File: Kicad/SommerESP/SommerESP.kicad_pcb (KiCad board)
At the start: 2 copper layers, 76.8 x 23.5 mm, 31 parts, among them J1 Serial programmer, J3 SOMMER CONEX BOARD, J4 SOMMER CONEX KEYPAD, J6 SOMMER OUTPUT OC, Q1 STN3NF06, Q2 2N7002DW, U4 LM2596SX-3.3/NOPB, U5 ESP32-C3-WROOM-02

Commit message: Fixed wrong LCSC number on the BOM
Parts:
- D1: value LED Green -> LED
- D2: value LED Blue -> LED
- turned C3 to 180 degrees

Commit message: Added 7.5mm position for J7 for more compatibility and updated the readme
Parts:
- added J7: SOMMER OUTPUT OC 7.5mm, Connector_PinSocket_2.54mm:PinSocket_1x04_P2.54mm_Vertical, B.Cu at (65.7, 36.7)
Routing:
- net GND: track 30.4 -> 32.4 mm
- net SommerSIG: track 7.28 -> 8.53 mm
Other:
- board text added: "7.5"
- board text added: "9.5"
- board text added: "SommerESP V3.1"
- board text added: "SommerESP v3.1"
- board text added: "X"
- board text removed: "SommerESP V3"
- board text removed: "SommerESP v3.0"

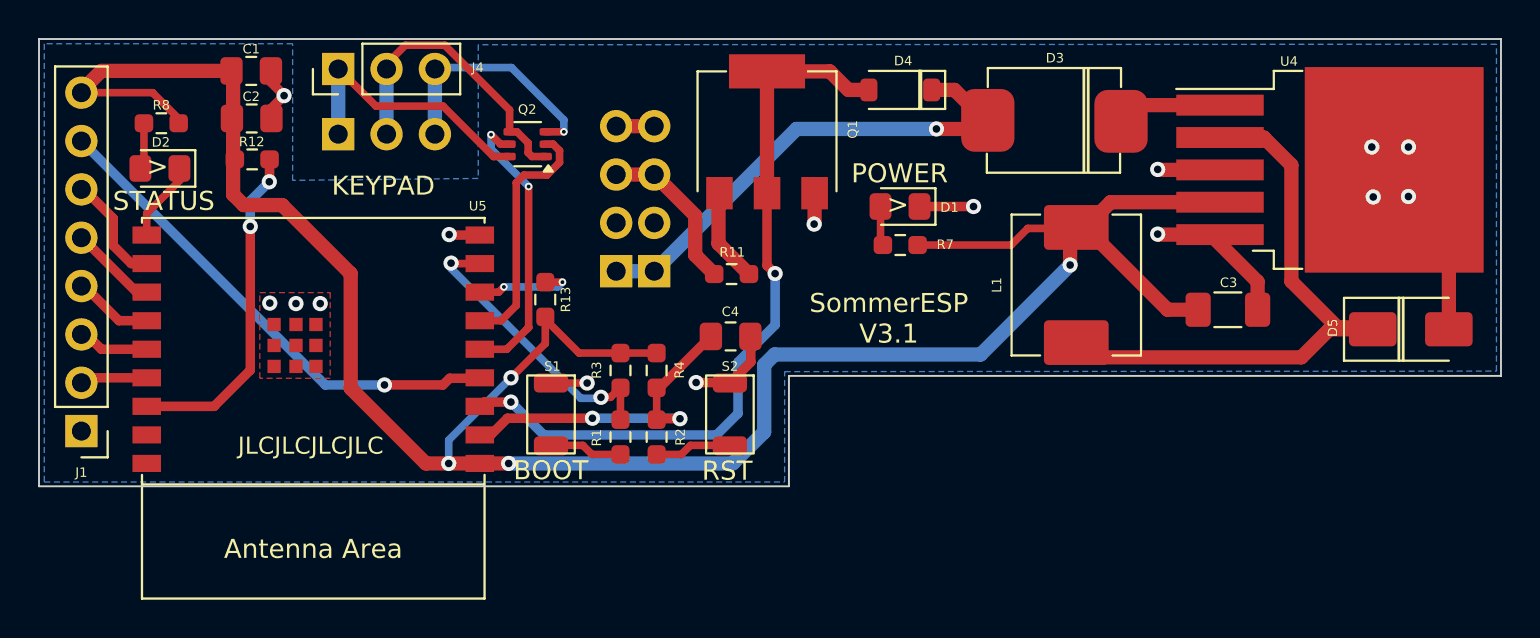
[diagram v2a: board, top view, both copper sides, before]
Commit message: Added fabrication holes on the PCB and setup up for production.
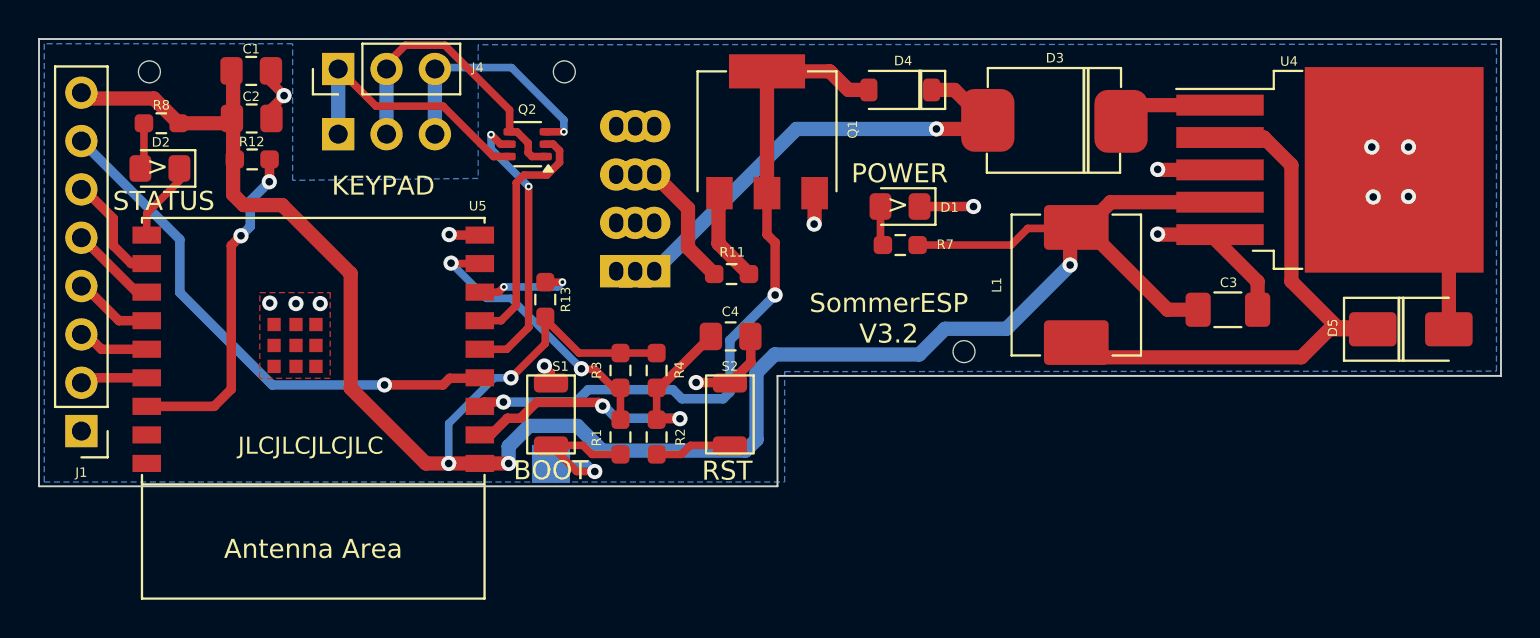
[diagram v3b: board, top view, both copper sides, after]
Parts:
- added H1: MountingHole, MountingHole:ToolingHole_1.152mm, F.Cu at (82.0, 40.9)
- added H2: MountingHole, MountingHole:ToolingHole_1.152mm, F.Cu at (39.2, 26.2)
- added H3: MountingHole, MountingHole:ToolingHole_1.152mm, F.Cu at (61.0, 26.2)
- added J8: SOMMER OUTPUT OC 8.5mm, SommerCustom:PinSocket_1x04_P2.54mm_Vertical_SLIT, B.Cu at (64.7, 36.7)
- added TP1: TestPoint, TestPoint:TestPoint_Pad_2.0x2.0mm, B.Cu at (60.3, 46.8)
- J6: value SOMMER OUTPUT OC -> SOMMER OUTPUT OC 9.5; footprint Connector_PinSocket_2.54mm:PinSocket_1x04_P2.54mm_Vertical -> SommerCustom:PinSocket_1x04_P2.54mm_Vertical_SLIT
- J7: footprint Connector_PinSocket_2.54mm:PinSocket_1x04_P2.54mm_Vertical -> SommerCustom:PinSocket_1x04_P2.54mm_Vertical_SLIT
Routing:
- net Net-(R1-Pad1): track 3.67 -> 9.00 mm, vias 0 -> 1
- net +3.3V: track 120.3 -> 117.2 mm
- net GND: track 32.4 -> 29.8 mm
- net AnalogSIG: track 37.6 -> 35.6 mm
- net IO5: track 26.1 -> 27.7 mm
- net EN: track 17.5 -> 18.2 mm
- net IO9: track 15.1 -> 14.6 mm
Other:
- outline, holes or cut-outs redrawn
- board text added: "8.5"
- board text added: "SommerESP V3.2"
- board text added: "SommerESP v3.2"
- board text removed: "SommerESP V3.1"
- board text removed: "SommerESP v3.1"

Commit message: Added RST pad
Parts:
- added TP2: RST, TestPoint:TestPoint_Pad_2.0x2.0mm, B.Cu at (69.7, 46.8)
- TP1: value TestPoint -> BOOT
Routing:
- net Net-(R2-Pad1): track 4.00 -> 8.45 mm, vias 0 -> 1
- net +3.3V: track 117.2 -> 115.4 mm
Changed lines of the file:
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@@
 		(embedded_fonts no)
 	)
+	(footprint "TestPoint:TestPoint_Pad_2.0x2.0mm"
+		(layer "B.Cu")
+		(at 69.725 46.825 180)
+		(descr "SMD rectangular pad as test Point, square 2.0mm side length")
+		(tags "test point SMD pad rectangle square")
+		(property "Reference" "TP2"
+			(at 0 1.998 0)
+			(layer "B.SilkS")
+			(hide yes)
+			(effects
+				(font
+					(size 1 1)
+					(thickness 0.15)
+				)
+				(justify mirror)
+			)
+		)
+		(property "Value" "RST"
+			(at 0 -2.05 0)
+			(layer "B.Fab")
+			(effects
+				(font
+					(size 1 1)
+					(thickness 0.15)
+				)
+				(justify mirror)
+			)
+		)
+		(property "Datasheet" ""
+			(at 0 0 0)
+			(unlocked yes)
+			(layer "B.Fab")
+			(hide yes)
+			(effects
+				(font
+					(size 1.27 1.27)
+					(thickness 0.15)
+				)
+				(justify mirror)
+			)
+		)
+		(property "Description" "test point"
+			(at 0 0 0)
+			(unlocked yes)
+			(layer "B.Fab")
+			(hide yes)
+			(effects
+				(font
+					(size 1.27 1.27)
+					(thickness 0.15)
+				)
+				(justify mirror)
+			)
+		)
+		(property ki_fp_filters "Pin* Test*")
+		(sheetname "/")
+		(sheetfile "SommerESP.kicad_sch")
+		(units
+			(unit
+				(name "A")
+				(pins "1")
+			)
+		)
+		(duplicate_pad_numbers_are_jumpers no)
+		(fp_line
+			(start 1.2 1.2)
+			(end 1.2 -1.2)
+			(stroke
+				(width 0.12)
+				(type solid)
+			)
+			(layer "B.SilkS")
+		)
+		(fp_line
+			(start 1.2 -1.2)
+			(end -1.2 -1.2)
+			(stroke
+				(width 0.12)
+				(type solid)
+			)
+			(layer "B.SilkS")
+		)
+		(fp_line
+			(start -1.2 1.2)
+			(end 1.2 1.2)
+			(stroke
+				(width 0.12)
+				(type solid)
+			)
+			(layer "B.SilkS")
+		)
+		(fp_line
+			(start -1.2 -1.2)
+			(end -1.2 1.2)
+			(stroke
+				(width 0.12)
+				(type solid)
+			)
+			(layer "B.SilkS")
+		)
+		(fp_line
+			(start 1.5 -1.5)
+			(end 1.5 1.5)
+			(stroke
+				(width 0.05)
+				(type solid)
+			)
+			(layer "B.CrtYd")
+		)
+		(fp_line
+			(start 1.5 -1.5)
+			(end -1.5 -1.5)
+			(stroke
+				(width 0.05)
+				(type solid)
+			)
+			(layer "B.CrtYd")
+		)
+		(fp_line
+			(start -1.5 1.5)
+			(end 1.5 1.5)
+			(stroke
+				(width 0.05)
+				(type solid)
+			)
+			(layer "B.CrtYd")
+		)
+		(fp_line
+			(start -1.5 1.5)
+			(end -1.5 -1.5)
+			(stroke
+				(width 0.05)
+				(type solid)
+			)
+			(layer "B.CrtYd")
+		)
+		(fp_text user "${REFERENCE}"
+			(at 0 2 0)
+			(layer "B.Fab")
+			(effects
+				(font
+					(size 1 1)
+					(thickness 0.15)
+				)
+				(justify mirror)
+			)
+		)
+		(pad "1" smd rect
+			(at 0 0 180)
+			(size 2 2)
+			(layers "B.Cu" "B.Mask")
+			(net "Net-(R2-Pad1)")
+			(pinfunction "1_1")
+			(pintype "passive")
+		)
+		(embedded_fonts no)
+	)
 	(footprint "LOGO"
 		(layer "B.Cu")
@@
 			)
 		)
-		(property "Value" "TestPoint"
+		(property "Value" "BOOT"
 			(at 0 -2.05 0)
 			(layer "B.Fab")
@@
 		)
 	)
-	(gr_text "BOOT\n"
-		(at 62.2 45.5 0)
-		(layer "B.SilkS")
-		(effects
-			(font
-				(size 1 1)
-				(thickness 0.15)
-			)
-			(justify left bottom mirror)
-		)
-	)
 	(gr_text "SommerESP v3.2\n"
-		(at 51.6 37.6 0)
+		(at 51.8 35.1 0)
 		(layer "B.SilkS")
 		(effects
@@
 	)
 	(segment
-		(start 71.1 42)
-		(end 72.05 41.05)
+		(start 68.45 44.8)
+		(end 69.5 44.8)
 		(width 0.75)
 		(layer "B.Cu")
@@
 	)
 	(segment
-		(start 62.986626 46.101)
-		(end 70.524 46.101)
+		(start 84.525 39.4)
+		(end 87.575 36.35)
 		(width 0.75)
 		(layer "B.Cu")
@@
 	)
 	(segment
-		(start 71.1 45.525)
-		(end 71.1 42)
+		(start 59.15 44.8)
+		(end 61.685626 44.8)
 		(width 0.75)
 		(layer "B.Cu")
@@
 	)
 	(segment
-		(start 61.685626 44.8)
-		(end 62.986626 46.101)
+		(start 69.5 44.8)
+		(end 71.1 43.2)
 		(width 0.75)
 		(layer "B.Cu")
@@
 	)
 	(segment
-		(start 58.075 45.875)
-		(end 59.15 44.8)
+		(start 61.685626 44.8)
+		(end 62.385626 45.5)
 		(width 0.75)
 		(layer "B.Cu")
@@
 	)
 	(segment
-		(start 58.075 46.775)
-		(end 58.075 45.875)
+		(start 79.65 41.05)
+		(end 81.3 39.4)
 		(width 0.75)
 		(layer "B.Cu")
@@
 	)
 	(segment
-		(start 81.001 39.699)
-		(end 84.226 39.699)
+		(start 81.3 39.4)
+		(end 84.525 39.4)
 		(width 0.75)
 		(layer "B.Cu")
@@
 	)
 	(segment
-		(start 59.15 44.8)
-		(end 61.685626 44.8)
+		(start 71.1 42)
+		(end 72.05 41.05)
 		(width 0.75)
 		(layer "B.Cu")
@@
 	)
 	(segment
+		(start 62.385626 45.5)
+		(end 67.75 45.5)
+		(width 0.75)
+		(layer "B.Cu")
+		(net "+3.3V")
+	)
+	(segment
 		(start 58.2 42.275)
 		(end 57.325 42.275)
@@
 	)
 	(segment
-		(start 79.65 41.05)
-		(end 81.001 39.699)
+		(start 72.05 41.05)
+		(end 79.65 41.05)
 		(width 0.75)
 		(layer "B.Cu")
@@
 	)
 	(segment
-		(start 70.524 46.101)
-		(end 71.1 45.525)
+		(start 67.75 45.5)
+		(end 68.45 44.8)
 		(width 0.75)
 		(layer "B.Cu")
@@
 	)
 	(segment
-		(start 72.05 41.05)
-		(end 79.65 41.05)
+		(start 57.325 42.275)
+		(end 54.925 44.675)
+		(width 0.4)
+		(layer "B.Cu")
+		(net "+3.3V")
+	)
+	(segment
+		(start 58.075 46.775)
+		(end 58.075 45.875)
 		(width 0.75)
 		(layer "B.Cu")
@@
 	)
 	(segment
-		(start 84.226 39.699)
-		(end 87.575 36.35)
+		(start 71.1 43.2)
+		(end 71.1 42)
 		(width 0.75)
 		(layer "B.Cu")
@@
 	)
 	(segment
-		(start 57.325 42.275)
-		(end 54.925 44.675)
-		(width 0.4)
+		(start 58.075 45.875)
+		(end 59.15 44.8)
+		(width 0.75)
 		(layer "B.Cu")
 		(net "+3.3V")
@@
 	)
 	(segment
+		(start 69.05 45.85)
+		(end 67.8 47.1)
+		(width 0.4)
+		(layer "F.Cu")
+		(net "Net-(R2-Pad1)")
+	)
+	(segment
 		(start 67.625 45.825)
 		(end 69.65 45.825)
@@
 		(net "Net-(R2-Pad1)")
 	)
+	(segment
+		(start 69.7 45.85)
+		(end 69.05 45.85)
+		(width 0.4)
+		(layer "F.Cu")
+		(net "Net-(R2-Pad1)")
+	)
+	(via
+		(at 67.8 47.1)
+		(size 0.8)
+		(drill 0.4)
+		(layers "F.Cu" "B.Cu")
+		(net "Net-(R2-Pad1)")
+	)
+	(segment
+		(start 69.45 47.1)
+		(end 69.725 46.825)
+		(width 0.4)
+		(layer "B.Cu")
+		(net "Net-(R2-Pad1)")
+	)
+	(segment
+		(start 67.8 47.1)
+		(end 69.45 47.1)
+		(width 0.4)
+		(layer "B.Cu")
+		(net "Net-(R2-Pad1)")
+	)
